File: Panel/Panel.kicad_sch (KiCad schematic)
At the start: 70 parts, among them J1 Conn_01x03, J10 Conn_01x02, J11 Conn_01x03, J12 Conn_01x03, J2 USB_C_Receptacle_USB2.0, J3 Conn_01x02, J4 Conn_02x06_Odd_Even, J5 Conn_01x07, J6 Conn_01x02, J7 Conn_01x02, J8 Conn_01x02, J9 Conn_01x02, SW1 SW_Push, SW2 SW_Push, U1 W25Q32JVSS, U2 RP2040, U3 NCP1117-3.3_SOT223, Y1 12.000MHz

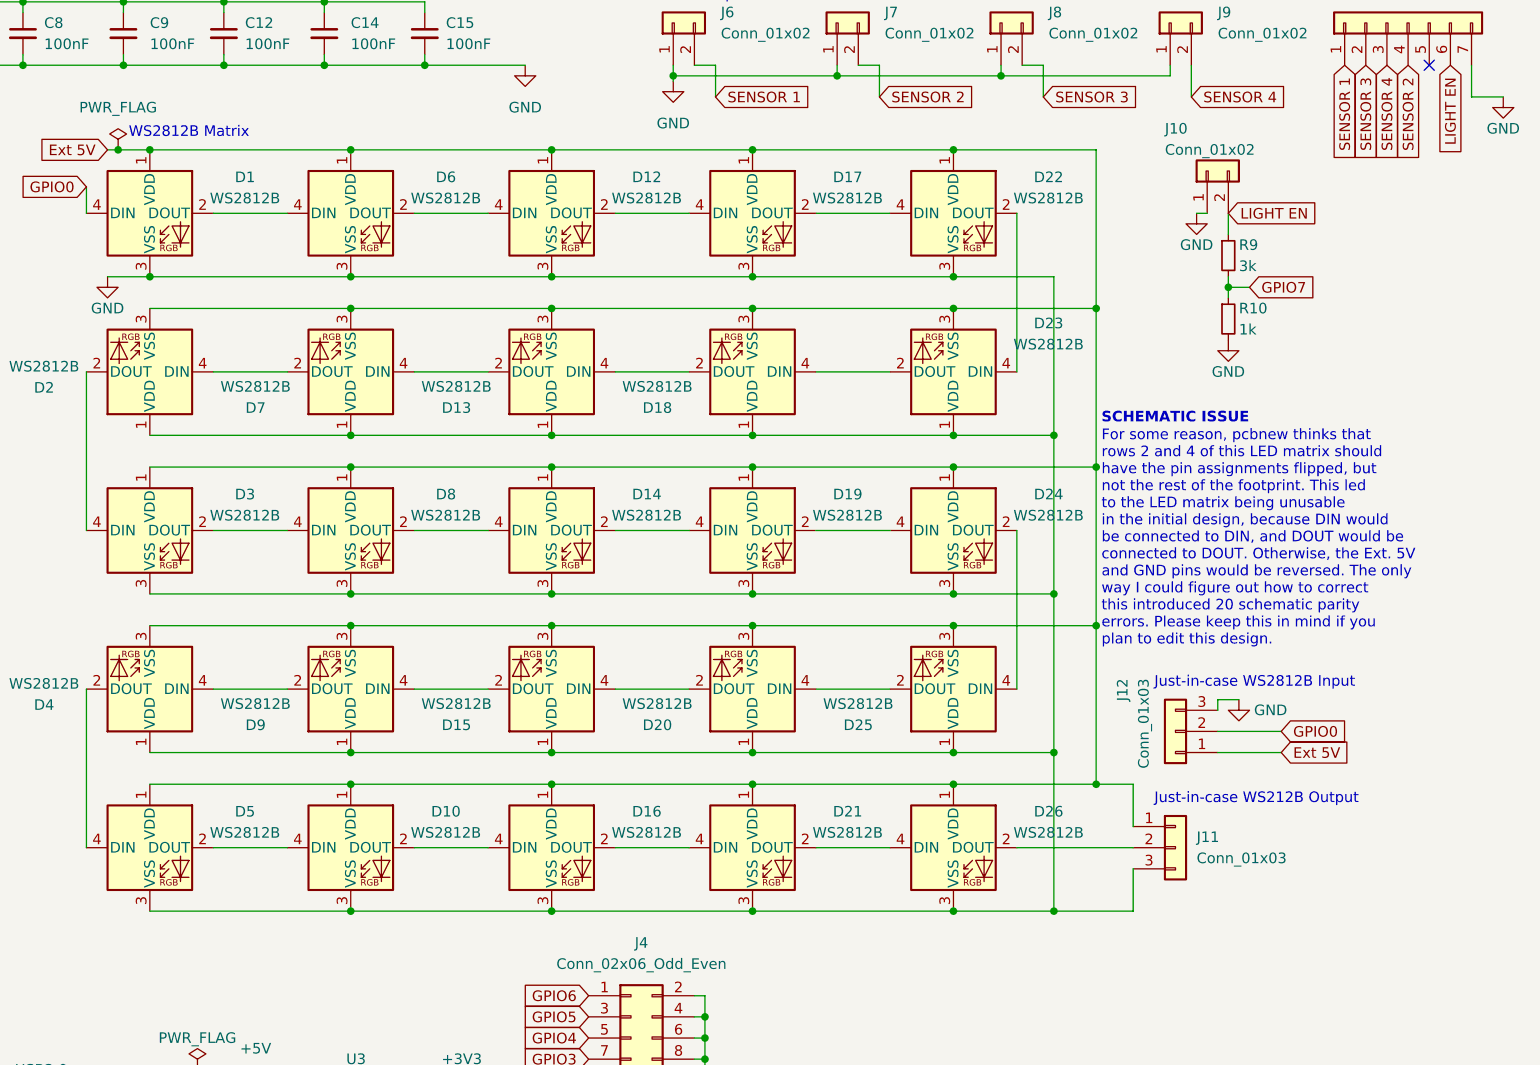
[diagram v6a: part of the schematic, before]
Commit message: Fix major schematic issue and parity warnings
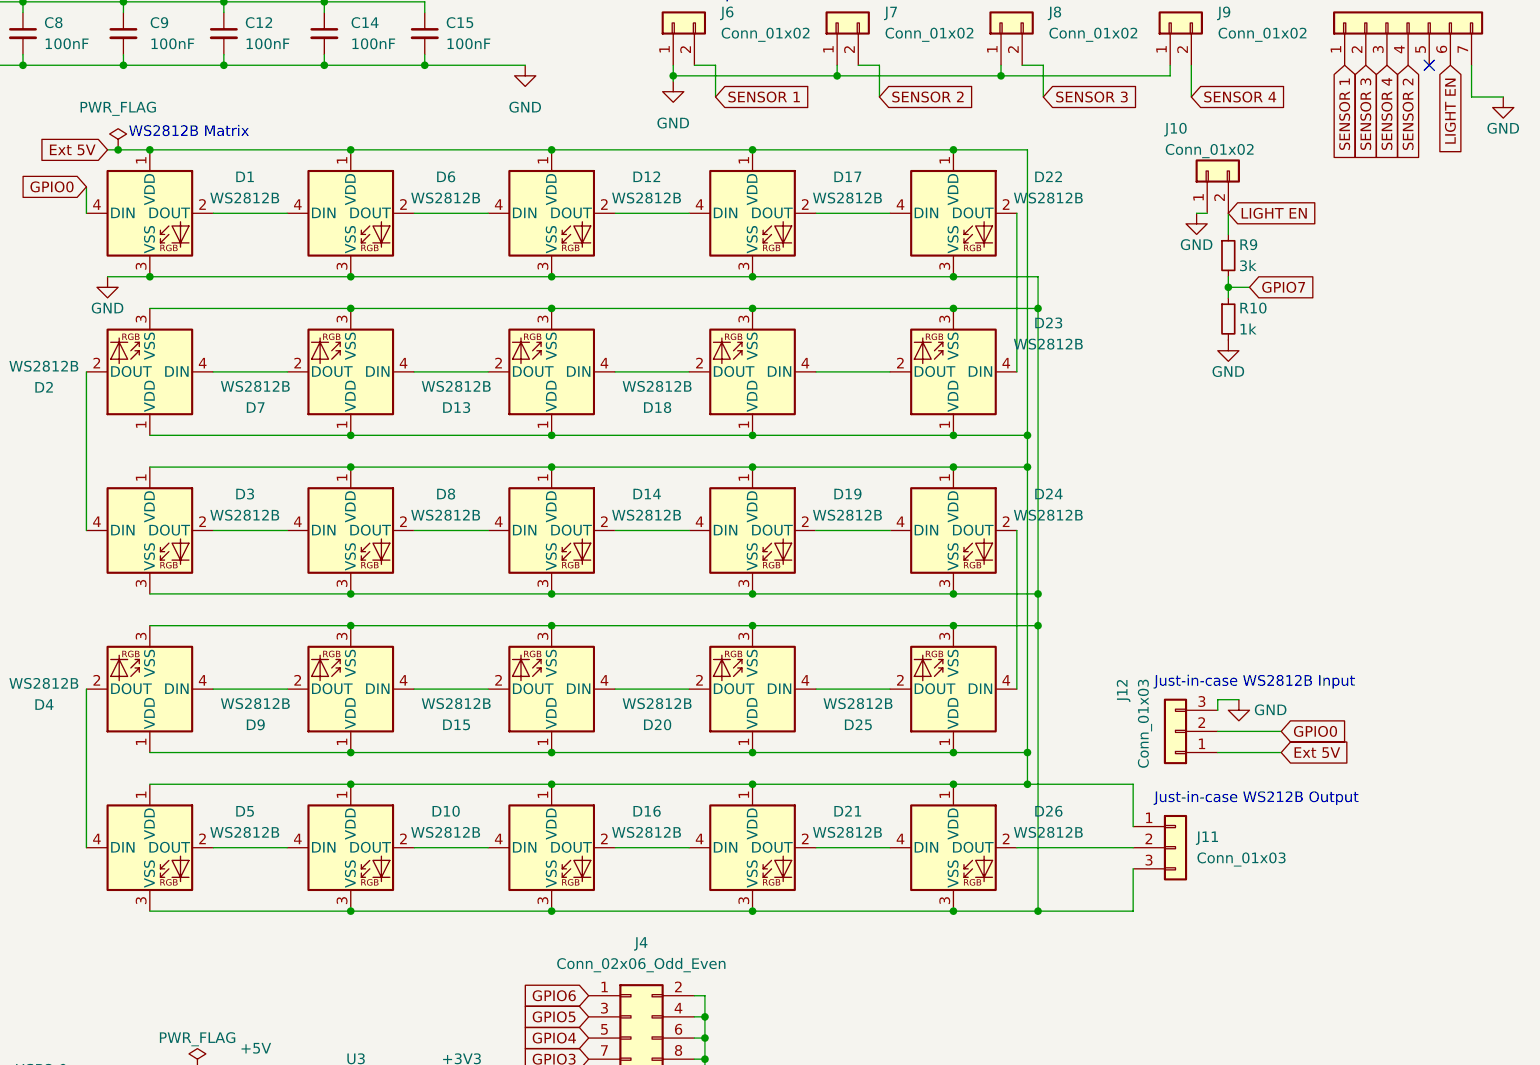
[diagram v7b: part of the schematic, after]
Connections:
- net Ext 5V: now also D13.1 (VDD), D15.1 (VDD), D18.1 (VDD), D2.1 (VDD), D20.1 (VDD), D23.1 (VDD), D25.1 (VDD), D4.1 (VDD), D7.1 (VDD), D9.1 (VDD); no longer D13.3 (VSS), D15.3 (VSS), D18.3 (VSS), D2.3 (VSS), D20.3 (VSS), D23.3 (VSS), D25.3 (VSS), D4.3 (VSS), D7.3 (VSS), D9.3 (VSS)
- net GND: now also D13.3 (VSS), D15.3 (VSS), D18.3 (VSS), D2.3 (VSS), D20.3 (VSS), D23.3 (VSS), D25.3 (VSS), D4.3 (VSS), D7.3 (VSS), D9.3 (VSS); no longer D13.1 (VDD), D15.1 (VDD), D18.1 (VDD), D2.1 (VDD), D20.1 (VDD), D23.1 (VDD), D25.1 (VDD), D4.1 (VDD), D7.1 (VDD), D9.1 (VDD)
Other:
- note removed: "For some reason, pcbnew thinks that rows 2 and 4 of this LED matrix should have the pin assignments flipped, but not the rest of the footprint. This led to the LED matrix being unusable in the initial design, because DIN would be connected to DIN, and DOUT would be connected to DOUT. Otherwise, the Ext. 5V and GND pins would be reversed. The only way I could figure out how to correct this introdu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"
- note removed: "SCHEMATIC ISSUE"

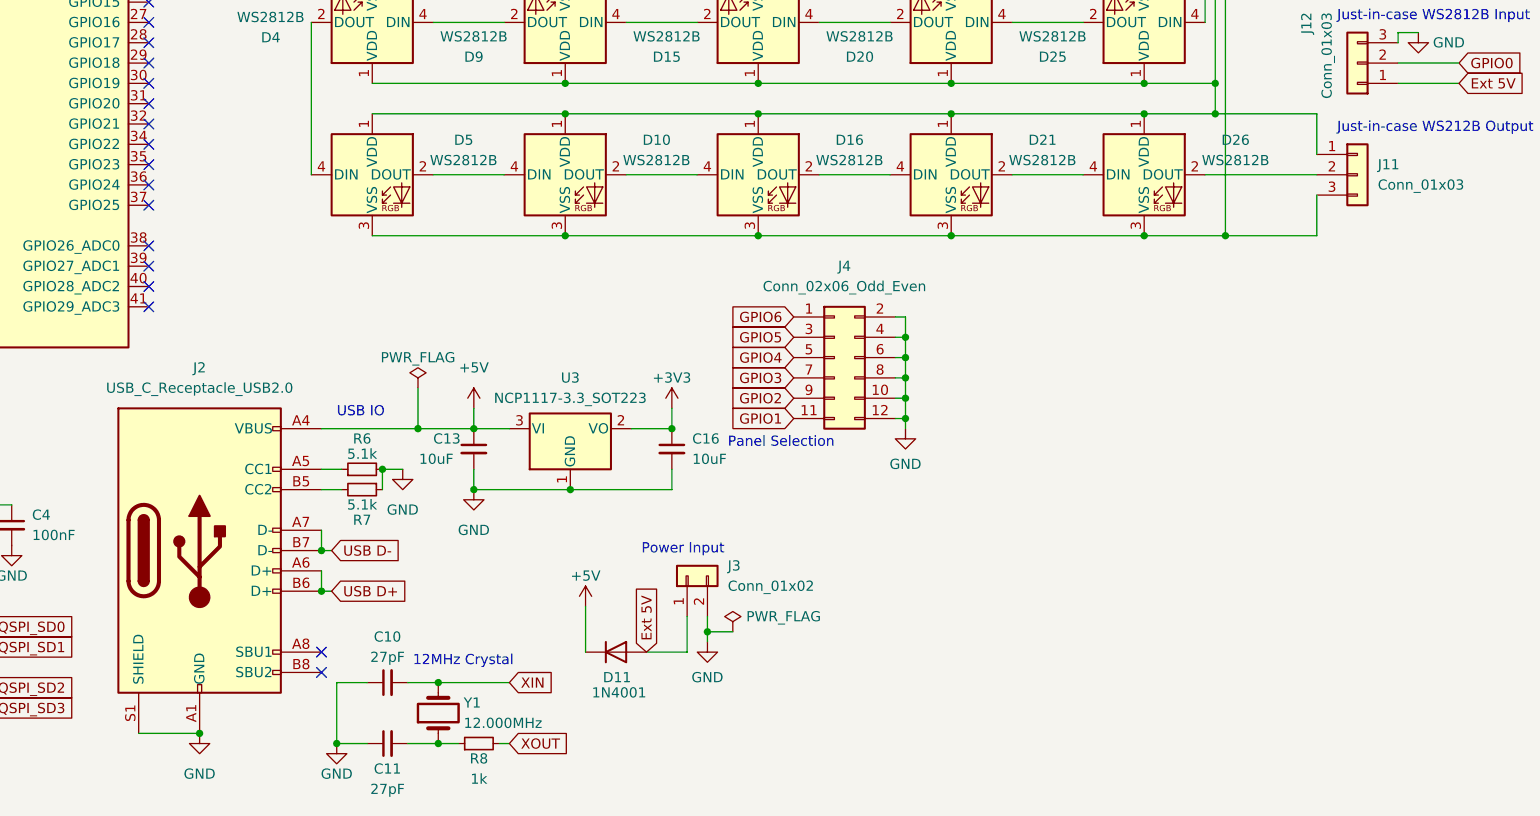
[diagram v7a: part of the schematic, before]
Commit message: Add USB protection, GP25 LED, silkscreen tweaks
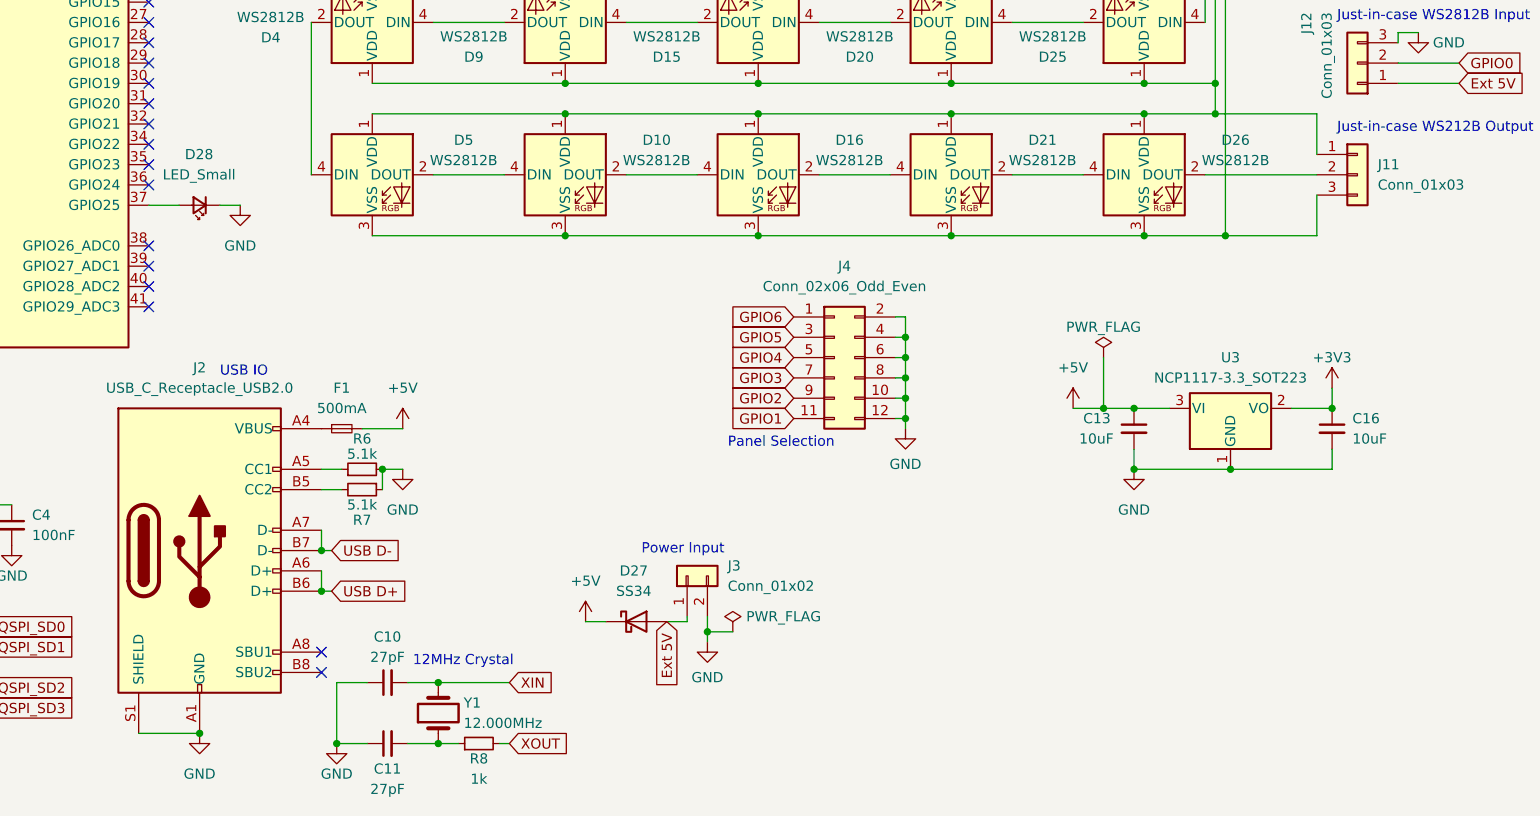
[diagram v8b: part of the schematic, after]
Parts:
- removed D11: 1N4001, Diode_THT:D_DO-41_SOD81_P10.16mm_Horizontal, symbol Diode:1N4001
- added D27: SS34, Diode_SMD:D_SMA_Handsoldering, symbol Device:D_Schottky
- added D28: LED_Small, LED_SMD:LED_0805_2012Metric_Pad1.15x1.40mm_HandSolder, symbol Device:LED_Small
- added F1: 500mA, Fuse:Fuse_1206_3216Metric_Pad1.42x1.75mm_HandSolder, symbol Device:Fuse_Small
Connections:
- net +5V: now also D27.1 (K), F1.2; no longer J2.A4 (VBUS), J2.A9 (VBUS), J2.B4 (VBUS), J2.B9 (VBUS)
- net Ext 5V: now also D27.2 (A)
- net GND: now also D28.1 (K)
- net at U2.37 (GPIO25): now also D28.2 (A)
- new net: F1.1, J2.A4 (VBUS), J2.A9 (VBUS), J2.B4 (VBUS), J2.B9 (VBUS)
- no-connect marks 25 -> 24
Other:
- moved on the sheet: C13, C16, U3
